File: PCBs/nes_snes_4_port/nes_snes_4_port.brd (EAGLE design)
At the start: 72.9 x 73.2 mm, 42 parts, among them J5 RJ45, J6 RJ45, J7 RJ45, J8 RJ45, J9 RJ45-S-4, U1 74245, U10 MC74VHC1GT125, U2 MC74VHC1GT125, U3 MC74VHC1GT125, U4 MC74VHC1GT125, U5 MC74VHC1GT125, U7 MC74VHC1GT125, U8 MC74VHC1GT125, U9 MC74VHC1GT125

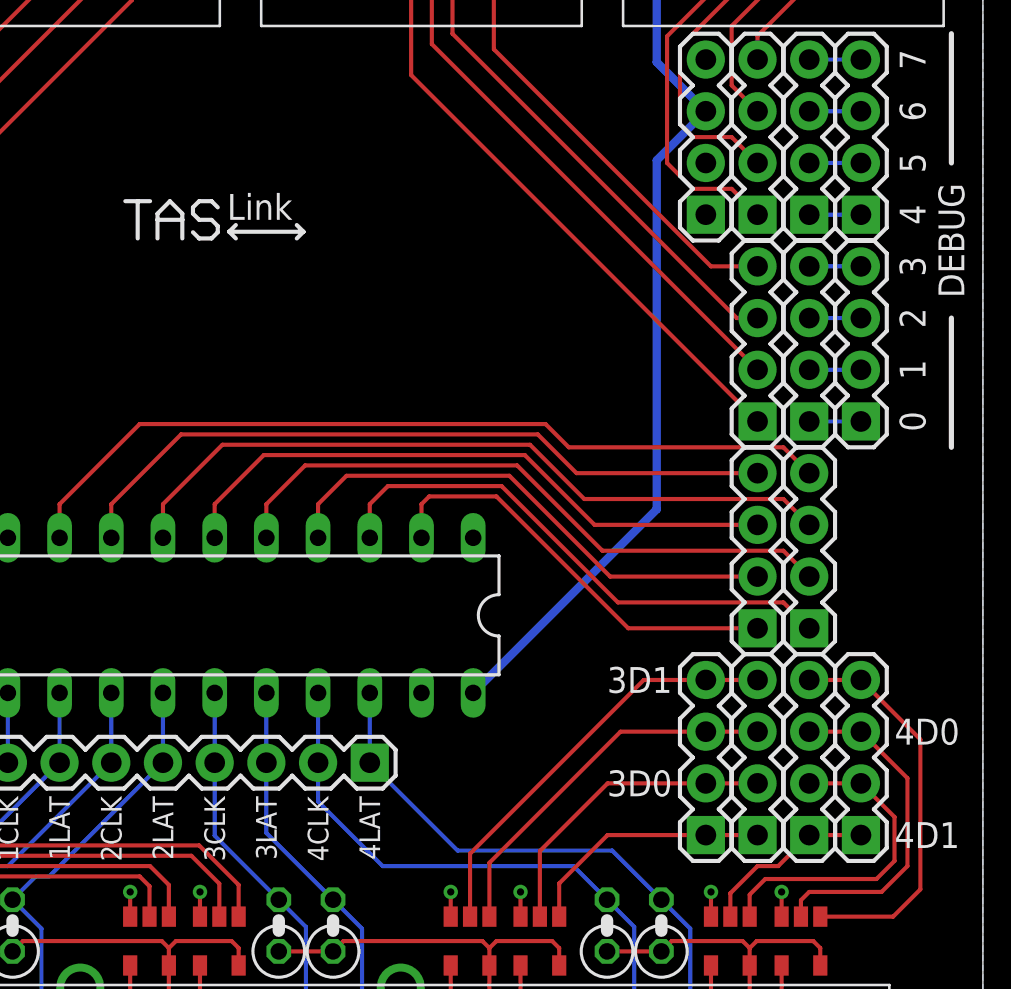
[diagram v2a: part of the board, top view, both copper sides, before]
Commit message: 4 port PCB: Cleaned up the schematic.
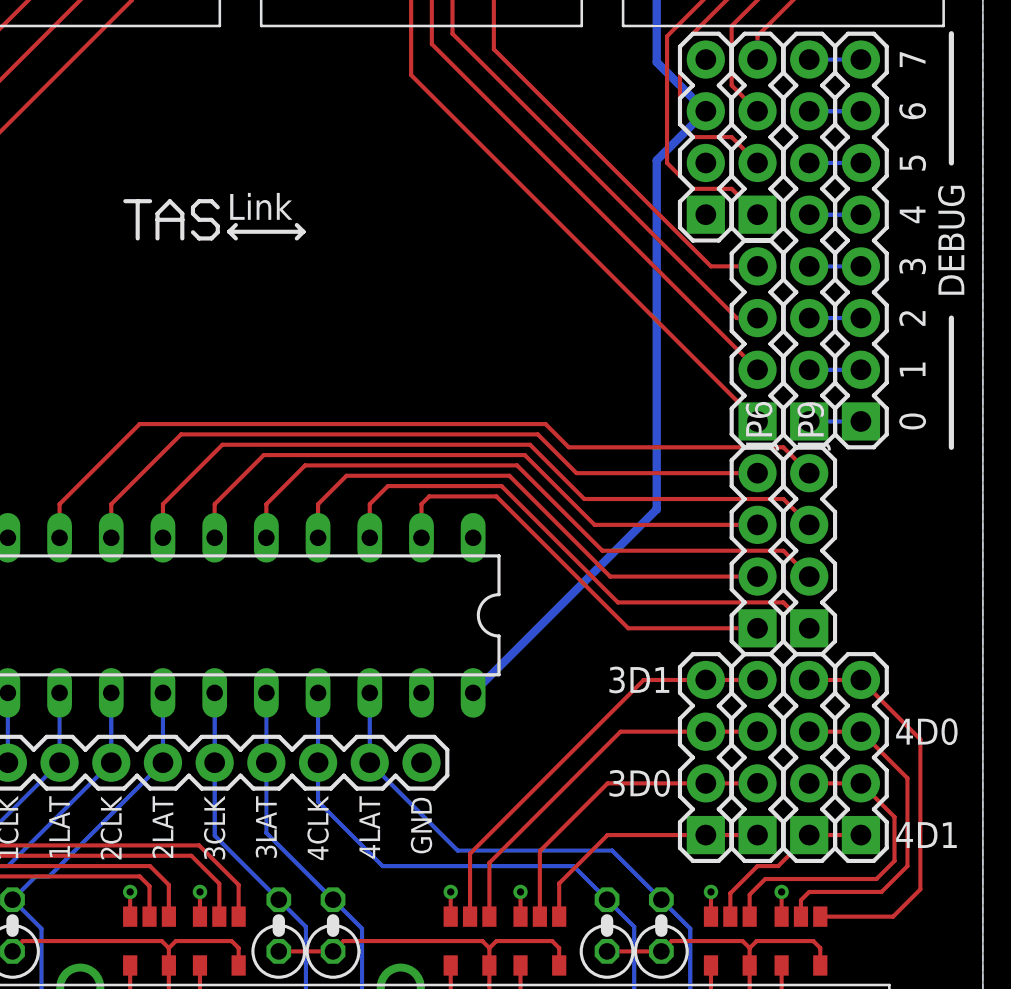
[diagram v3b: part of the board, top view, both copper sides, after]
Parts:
- removed JP10, JP2, JP3: (no value), SparkFun-Connectors:1X04
- added JP21: M09, SparkFun-Connectors:1X09
- JP9: device SparkFun-Connectors:1X04 -> SparkFun-Connectors:1X08
- moved JP6 27.3 mm to (64.8, 40.9), turned to 90 degrees
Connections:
- net CP1_CLOCK: now also JP21.9; no longer JP6.8
- net CP1_LATCH: now also JP21.8; no longer JP6.7
- net CP2_CLOCK: now also JP21.7; no longer JP6.6
- net CP2_LATCH: now also JP21.6; no longer JP6.5
- net CP3_CLOCK: now also JP21.5; no longer JP6.4
- net CP3_LATCH: now also JP21.4; no longer JP6.3
- net CP4_CLOCK: now also JP21.3; no longer JP6.2
- net CP4_LATCH: now also JP21.2; no longer JP6.1
- net DEBUG0: now also JP6.1, JP9.1; no longer JP2.4, JP9.4
- net DEBUG1: now also JP6.2, JP9.2; no longer JP2.3, JP9.3
- net DEBUG2: now also JP6.3, JP9.3; no longer JP2.2, JP9.2
- net DEBUG3: now also JP6.4, JP9.4; no longer JP2.1, JP9.1
- net DEBUG4: now also JP6.5, JP9.5; no longer JP10.4, JP3.4
- net DEBUG5: now also JP6.6, JP9.6; no longer JP10.3, JP3.3
- net DEBUG6: now also JP6.7, JP9.7; no longer JP10.2, JP3.2
- net DEBUG7: now also JP6.8, JP9.8; no longer JP10.1, JP3.1
- net GND: now also JP21.1
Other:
- board text added: "GND"
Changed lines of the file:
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@@
 <text x="58.039" y="28.194" size="1.27" layer="21" font="vector" ratio="16" rot="R180" align="center-left">3D1</text>
 <text x="58.039" y="23.114" size="1.27" layer="21" font="vector" ratio="16" rot="R180" align="center-left">3D0</text>
+<text x="45.72" y="22.479" size="1.016" layer="21" font="vector" ratio="16" rot="R270" align="center-left">GND</text>
 </plain>
 <attributes>
@@
 <elements>
 <element name="U1" library="TASLink" package="DIL20" value="74245" x="36.83" y="31.369" smashed="yes" rot="R180"/>
-<element name="JP2" library="SparkFun-Connectors" package="1X04" value="" x="64.77" y="40.894" smashed="yes" rot="R90">
-<attribute name="VALUE" x="67.945" y="39.624" size="1.27" layer="27" rot="R90"/>
-</element>
-<element name="JP3" library="SparkFun-Connectors" package="1X04" value="" x="64.77" y="51.054" smashed="yes" rot="R90">
-<attribute name="VALUE" x="67.945" y="49.784" size="1.27" layer="27" rot="R90"/>
-</element>
 <element name="R1" library="rcl" package="0207/2V" value="3.6k" x="7.5946" y="16.129" smashed="yes" rot="R90"/>
 <element name="R2" library="rcl" package="0207/2V" value="3.6k" x="22.9616" y="16.129" smashed="yes" rot="R90"/>
@@
 <element name="JP7" library="SparkFun-Connectors" package="1X04" value="" x="62.23" y="30.734" smashed="yes" rot="R90">
 <attribute name="VALUE" x="65.405" y="29.464" size="1.27" layer="27" rot="R90"/>
-</element>
-<element name="JP9" library="SparkFun-Connectors" package="1X04" value="" x="67.31" y="40.894" smashed="yes" rot="R90">
-<attribute name="VALUE" x="70.485" y="39.624" size="1.27" layer="27" rot="R90"/>
-</element>
-<element name="JP10" library="SparkFun-Connectors" package="1X04" value="" x="67.31" y="51.054" smashed="yes" rot="R90">
-<attribute name="VALUE" x="70.485" y="49.784" size="1.27" layer="27" rot="R90"/>
 </element>
 <element name="U7" library="TASLink" package="TSOP-5" value="MC74VHC1GT125" x="51.5366" y="15.367" smashed="yes"/>
@@
 <element name="J7" library="TASLink" package="RJ45" value="RJ45" x="45.72" y="66.802" smashed="yes" rot="R180"/>
 <element name="J8" library="TASLink" package="RJ45" value="RJ45" x="63.5" y="66.802" smashed="yes" rot="R180"/>
-<element name="JP6" library="SparkFun-Connectors" package="1X08" value="" x="43.18" y="24.13" smashed="yes" rot="R180">
-<attribute name="VALUE" x="44.45" y="27.305" size="1.27" layer="27" rot="R180"/>
-</element>
 <element name="JP5" library="SparkFun-Connectors" package="1X08" value="" x="8.89" y="20.574" smashed="yes" rot="R90">
 <attribute name="VALUE" x="12.065" y="19.304" size="1.27" layer="27" rot="R90"/>
@@
 <attribute name="VALUE" x="70.485" y="19.304" size="1.27" layer="27" rot="R90"/>
 </element>
+<element name="JP21" library="SparkFun-Connectors" package="1X09" value="M09" x="45.72" y="24.13" smashed="yes" rot="R180">
+<attribute name="VALUE" x="46.99" y="27.305" size="1.27" layer="27" rot="R180"/>
+</element>
+<element name="JP6" library="SparkFun-Connectors" package="1X08" value="" x="64.77" y="40.894" rot="R90"/>
+<element name="JP9" library="SparkFun-Connectors" package="1X08" value="" x="67.31" y="40.894" rot="R90"/>
 </elements>
 <signals>
@@
 <via x="59.944" y="17.78" extent="1-16" drill="0.3556"/>
 <via x="63.4136" y="17.78" extent="1-16" drill="0.3556"/>
+<contactref element="JP21" pad="1"/>
 </signal>
 <signal name="CP1_+5V">
@@
 <contactref element="U1" pad="12"/>
 <contactref element="R3" pad="2"/>
-<contactref element="JP6" pad="7"/>
 <contactref element="J9" pad="1-6"/>
 <wire x1="11.684" y1="7.239" x2="11.684" y2="15.9766" width="0.2032" layer="16"/>
@@
 <wire x1="11.4046" y1="18.542" x2="22.352" y2="18.542" width="0.2032" layer="16"/>
 <wire x1="22.352" y1="18.542" x2="27.94" y2="24.13" width="0.2032" layer="16"/>
+<contactref element="JP21" pad="8"/>
 </signal>
 <signal name="CP1_CLOCK">
 <contactref element="U1" pad="11"/>
 <contactref element="R1" pad="2"/>
-<contactref element="JP6" pad="8"/>
 <contactref element="J9" pad="1-8"/>
 <wire x1="8.9281" y1="7.9629" x2="8.9281" y2="16.0655" width="0.2032" layer="16"/>
@@
 <wire x1="9.652" y1="7.239" x2="8.9281" y2="7.9629" width="0.2032" layer="16"/>
 <wire x1="8.9281" y1="16.0655" x2="7.5946" y2="17.399" width="0.2032" layer="16"/>
+<contactref element="JP21" pad="9"/>
 </signal>
 <signal name="CP2_IODATA">
@@
 <contactref element="U1" pad="14"/>
 <contactref element="R4" pad="2"/>
-<contactref element="JP6" pad="5"/>
 <contactref element="J9" pad="2-6"/>
 <wire x1="33.02" y1="27.559" x2="33.02" y2="24.13" width="0.2032" layer="16"/>
@@
 <wire x1="26.7716" y1="18.542" x2="27.432" y2="18.542" width="0.2032" layer="16"/>
 <wire x1="27.432" y1="18.542" x2="33.02" y2="24.13" width="0.2032" layer="16"/>
+<contactref element="JP21" pad="6"/>
 </signal>
 <signal name="CP2_CLOCK">
 <contactref element="U1" pad="13"/>
 <contactref element="R2" pad="2"/>
-<contactref element="JP6" pad="6"/>
 <contactref element="J9" pad="2-8"/>
 <wire x1="30.48" y1="27.559" x2="30.48" y2="24.13" width="0.2032" layer="16"/>
@@
 <wire x1="24.6126" y1="19.05" x2="25.4" y2="19.05" width="0.2032" layer="16"/>
 <wire x1="25.4" y1="19.05" x2="30.48" y2="24.13" width="0.2032" layer="16"/>
+<contactref element="JP21" pad="7"/>
 </signal>
 <signal name="CP1_CLOCK_LV">
@@
 </signal>
 <signal name="DEBUG0">
-<contactref element="JP2" pad="4"/>
+<contactref element="JP6" pad="1"/>
+<contactref element="JP9" pad="1"/>
+<wire x1="64.77" y1="40.894" x2="67.31" y2="40.894" width="0.2032" layer="16"/>
+</signal>
+<signal name="DEBUG1">
+<contactref element="JP6" pad="2"/>
+<contactref element="JP9" pad="2"/>
+<wire x1="64.77" y1="43.434" x2="67.31" y2="43.434" width="0.2032" layer="16"/>
+</signal>
+<signal name="DEBUG2">
+<contactref element="JP6" pad="3"/>
+<contactref element="JP9" pad="3"/>
+<wire x1="64.77" y1="45.974" x2="67.31" y2="45.974" width="0.2032" layer="16"/>
+</signal>
+<signal name="DEBUG3">
+<contactref element="JP6" pad="4"/>
 <contactref element="JP9" pad="4"/>
 <wire x1="64.77" y1="48.514" x2="67.31" y2="48.514" width="0.2032" layer="16"/>
 </signal>
-<signal name="DEBUG1">
-<contactref element="JP2" pad="3"/>
-<contactref element="JP9" pad="3"/>
-<wire x1="64.77" y1="45.974" x2="67.31" y2="45.974" width="0.2032" layer="16"/>
-</signal>
-<signal name="DEBUG2">
-<contactref element="JP2" pad="2"/>
-<contactref element="JP9" pad="2"/>
-<wire x1="64.77" y1="43.434" x2="67.31" y2="43.434" width="0.2032" layer="16"/>
-</signal>
-<signal name="DEBUG3">
-<contactref element="JP2" pad="1"/>
-<contactref element="JP9" pad="1"/>
-<wire x1="64.77" y1="40.894" x2="67.31" y2="40.894" width="0.2032" layer="16"/>
-</signal>
 <signal name="DEBUG4">
-<contactref element="JP3" pad="4"/>
-<contactref element="JP10" pad="4"/>
+<contactref element="JP6" pad="5"/>
+<contactref element="JP9" pad="5"/>
+<wire x1="64.77" y1="51.054" x2="67.31" y2="51.054" width="0.2032" layer="16"/>
+</signal>
+<signal name="DEBUG5">
+<contactref element="JP6" pad="6"/>
+<contactref element="JP9" pad="6"/>
+<wire x1="64.77" y1="53.594" x2="67.31" y2="53.594" width="0.2032" layer="16"/>
+</signal>
+<signal name="DEBUG6">
+<contactref element="JP6" pad="7"/>
+<contactref element="JP9" pad="7"/>
+<wire x1="64.77" y1="56.134" x2="67.31" y2="56.134" width="0.2032" layer="16"/>
+</signal>
+<signal name="DEBUG7">
+<contactref element="JP6" pad="8"/>
+<contactref element="JP9" pad="8"/>
 <wire x1="64.77" y1="58.674" x2="67.31" y2="58.674" width="0.2032" layer="16"/>
-</signal>
-<signal name="DEBUG5">
-<contactref element="JP3" pad="3"/>
-<contactref element="JP10" pad="3"/>
-<wire x1="64.77" y1="56.134" x2="67.31" y2="56.134" width="0.2032" layer="16"/>
-</signal>
-<signal name="DEBUG6">
-<contactref element="JP3" pad="2"/>
-<contactref element="JP10" pad="2"/>
-<wire x1="64.77" y1="53.594" x2="67.31" y2="53.594" width="0.2032" layer="16"/>
-</signal>
-<signal name="DEBUG7">
-<contactref element="JP3" pad="1"/>
-<contactref element="JP10" pad="1"/>
-<wire x1="64.77" y1="51.054" x2="67.31" y2="51.054" width="0.2032" layer="16"/>
 </signal>
 <signal name="CP2_+5V">
@@
 <contactref element="R11" pad="2"/>
 <contactref element="U1" pad="16"/>
-<contactref element="JP6" pad="3"/>
 <contactref element="J9" pad="3-6"/>
 <wire x1="38.1" y1="27.559" x2="38.1" y2="24.13" width="0.2032" layer="16"/>
@@
 <wire x1="41.3766" y1="17.399" x2="38.1" y2="20.6756" width="0.2032" layer="16"/>
 <wire x1="38.1" y1="20.6756" x2="38.1" y2="24.13" width="0.2032" layer="16"/>
+<contactref element="JP21" pad="4"/>
 </signal>
 <signal name="CP3_CLOCK">
 <contactref element="R5" pad="2"/>
 <contactref element="U1" pad="15"/>
-<contactref element="JP6" pad="4"/>
 <contactref element="J9" pad="3-8"/>
 <wire x1="35.56" y1="27.559" x2="35.56" y2="24.13" width="0.2032" layer="16"/>
@@
 <wire x1="38.7096" y1="17.399" x2="35.56" y2="20.5486" width="0.2032" layer="16"/>
 <wire x1="35.56" y1="20.5486" x2="35.56" y2="24.13" width="0.2032" layer="16"/>
+<contactref element="JP21" pad="5"/>
 </signal>
 <signal name="CP4_+5V">
@@
 <contactref element="R12" pad="2"/>
 <contactref element="U1" pad="18"/>
-<contactref element="JP6" pad="1"/>
 <contactref element="J9" pad="4-6"/>
 <wire x1="43.18" y1="27.559" x2="43.18" y2="24.13" width="0.2032" layer="16"/>
@@
 <wire x1="55.0926" y1="19.812" x2="47.498" y2="19.812" width="0.2032" layer="16"/>
 <wire x1="47.498" y1="19.812" x2="43.18" y2="24.13" width="0.2032" layer="16"/>
+<contactref element="JP21" pad="2"/>
 </signal>
 <signal name="CP4_CLOCK">
 <contactref element="R6" pad="2"/>
 <contactref element="U1" pad="17"/>
-<contactref element="JP6" pad="2"/>
 <contactref element="J9" pad="4-8"/>
 <wire x1="40.64" y1="27.559" x2="40.64" y2="24.13" width="0.2032" layer="16"/>
@@
 <wire x1="43.815" y1="19.05" x2="40.64" y2="22.225" width="0.2032" layer="16"/>
 <wire x1="40.64" y1="22.225" x2="40.64" y2="24.13" width="0.2032" layer="16"/>
+<contactref element="JP21" pad="3"/>
 </signal>
 <signal name="CP3_CLOCK_LV">
